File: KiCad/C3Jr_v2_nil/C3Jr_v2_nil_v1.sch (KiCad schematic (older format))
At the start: 49 parts, among them K1 CONN_3, P10 CONN_1, P3 A_IN, P36 DIL6, P37 DIL6, P38 DIL6, P39 DIL6, P4 ISP, P6 STACK-R, P7 DC_IN_1, P8 DC_IN_2, P9 CONN_1, Q1 PNP, U1 ATTINY85-P, X1 CRYSTAL2

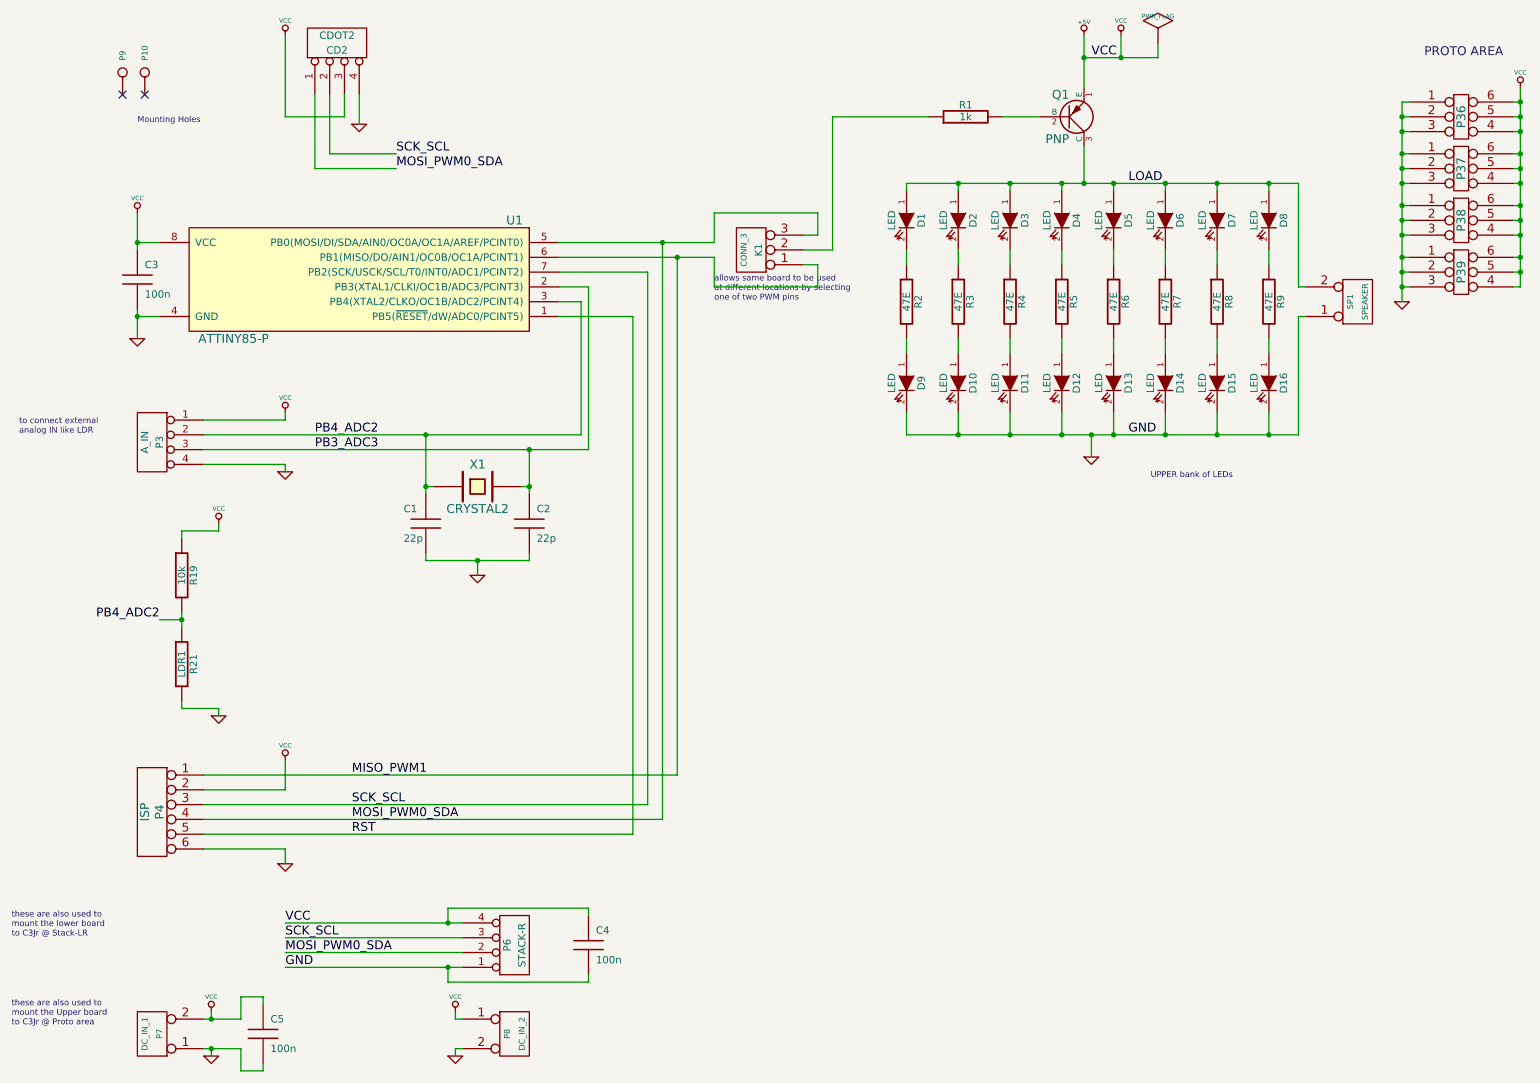
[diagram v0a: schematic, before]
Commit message: C3Jr_v2_nil - revised PCB , smaller size
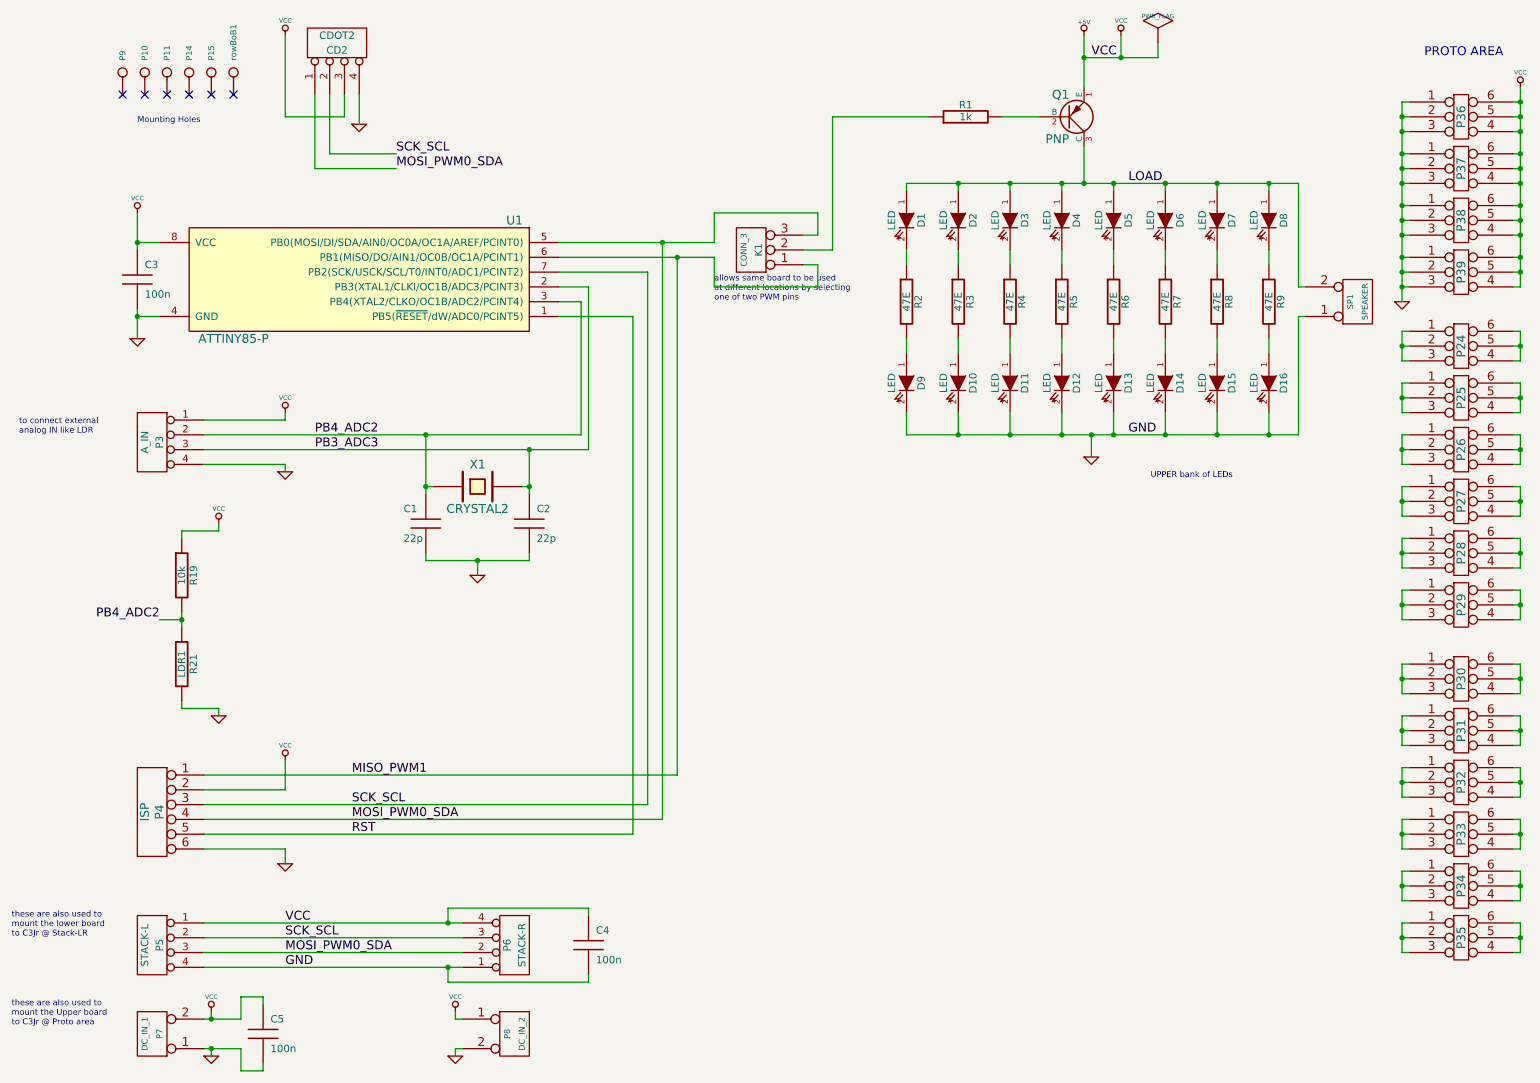
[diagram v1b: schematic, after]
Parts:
- added P11, P14, P15, rowBoB1: CONN_1, symbol CONN_1
- added P24, P25, P26, P27, P28, P29, P30, P31, P32, P33, P34, P35: DIL6, PROTO-6, symbol DIL6
- added P5: STACK-L, symbol CONN_4
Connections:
- net +5V: now also P5.1 (P1)
- net GND: now also P5.4 (P4)
- net MOSI_PWM0_SDA: now also P5.3 (P3)
- net SCK_SCL: now also P5.2 (P2)
- new net: P29.1 (P1), P29.2 (P2), P29.3 (P3)
- new net: P29.4 (P4), P29.5 (P5), P29.6 (P6)
- new net: P28.1 (P1), P28.2 (P2), P28.3 (P3)
- new net: P28.4 (P4), P28.5 (P5), P28.6 (P6)
- new net: P27.1 (P1), P27.2 (P2), P27.3 (P3)
- new net: P27.4 (P4), P27.5 (P5), P27.6 (P6)
- new net: P26.1 (P1), P26.2 (P2), P26.3 (P3)
- new net: P26.4 (P4), P26.5 (P5), P26.6 (P6)
- new net: P25.1 (P1), P25.2 (P2), P25.3 (P3)
- new net: P25.4 (P4), P25.5 (P5), P25.6 (P6)
- new net: P24.1 (P1), P24.2 (P2), P24.3 (P3)
- new net: P24.4 (P4), P24.5 (P5), P24.6 (P6)
- new net: P35.1 (P1), P35.2 (P2), P35.3 (P3)
- new net: P35.4 (P4), P35.5 (P5), P35.6 (P6)
- new net: P34.1 (P1), P34.2 (P2), P34.3 (P3)
- new net: P34.4 (P4), P34.5 (P5), P34.6 (P6)
- new net: P33.1 (P1), P33.2 (P2), P33.3 (P3)
- new net: P33.4 (P4), P33.5 (P5), P33.6 (P6)
- new net: P32.1 (P1), P32.2 (P2), P32.3 (P3)
- new net: P32.4 (P4), P32.5 (P5), P32.6 (P6)
- new net: P31.1 (P1), P31.2 (P2), P31.3 (P3)
- new net: P31.4 (P4), P31.5 (P5), P31.6 (P6)
- new net: P30.1 (P1), P30.2 (P2), P30.3 (P3)
- new net: P30.4 (P4), P30.5 (P5), P30.6 (P6)
- no-connect marks 2 -> 6
